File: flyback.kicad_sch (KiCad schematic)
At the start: 47 parts, among them Q2001 FDC86244, U2001 TPS23751PWP, U2002 TCMT1107, U2003 TLV431ACDBZR

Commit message: Updating layout
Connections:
- net T_PRI: now reaches C2003.1, C2004.1, CR2001.1, L2001.2, R2002.1, R2005.1, R2007.1, T2001.1
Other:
- moved on the sheet: C2002
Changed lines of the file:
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@@
 	)
 	(junction
+		(at 95.25 57.15)
+		(diameter 0)
+		(color 0 0 0 0)
+	)
+	(junction
 		(at 195.58 125.73)
 		(diameter 0)
@@
 	)
 	(junction
-		(at 97.79 57.15)
-		(diameter 0)
-		(color 0 0 0 0)
-	)
-	(junction
 		(at 180.34 57.15)
 		(diameter 0)
@@
 	(wire
 		(pts
-			(xy 97.79 40.64) (xy 97.79 44.45)
+			(xy 95.25 40.64) (xy 95.25 44.45)
 		)
 		(stroke
@@
 	(wire
 		(pts
+			(xy 95.25 57.15) (xy 105.41 57.15)
+		)
+		(stroke
+			(width 0)
+			(type default)
+		)
+	)
+	(wire
+		(pts
 			(xy 83.82 139.7) (xy 52.07 139.7)
 		)
@@
 	(wire
 		(pts
-			(xy 102.87 40.64) (xy 97.79 40.64)
+			(xy 102.87 40.64) (xy 95.25 40.64)
 		)
 		(stroke
@@
 	(wire
 		(pts
-			(xy 97.79 57.15) (xy 105.41 57.15)
-		)
-		(stroke
-			(width 0)
-			(type default)
-		)
-	)
-	(wire
-		(pts
 			(xy 50.8 121.92) (xy 50.8 124.46)
 		)
@@
 	(wire
 		(pts
-			(xy 45.72 57.15) (xy 97.79 57.15)
+			(xy 45.72 57.15) (xy 95.25 57.15)
 		)
 		(stroke
@@
 		)
 	)
+	(label "T_PRI"
+		(at 207.01 57.15 0)
+		(fields_autoplaced yes)
+		(effects
+			(font
+				(size 1.27 1.27)
+			)
+			(justify left bottom)
+		)
+	)
 	(global_label "APD"
 		(shape input)
@@
 	(symbol
 		(lib_id "PoE-rescue:C-pspice")
-		(at 97.79 50.8 0)
+		(at 95.25 50.8 0)
 		(mirror x)
 		(unit 1)
@@
 		(dnp no)
 		(property "Reference" "C2002"
-			(at 102.3112 51.9684 0)
+			(at 99.7712 51.9684 0)
 			(effects
 				(font
@@
 		)
 		(property "Value" "22u"
-			(at 102.3112 49.657 0)
+			(at 99.7712 49.657 0)
 			(effects
 				(font
@@
 		)
 		(property "Footprint" "footprints:CAP_WCAP-ASLI_06p3X05p5_WRE"
-			(at 97.79 50.8 0)
+			(at 95.25 50.8 0)
 			(effects
 				(font
@@
 		)
 		(property "Datasheet" "~"
-			(at 97.79 50.8 0)
+			(at 95.25 50.8 0)
 			(effects
 				(font
@@
 		)
 		(property "Description" "CIN1"
-			(at 102.362 47.498 0)
+			(at 99.822 47.498 0)
 			(effects
 				(font

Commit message: Added routing
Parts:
- C2002: value 22u -> 47u; Voltage (none) -> 100V
- C2003: footprint footprints:CAP_WCAP-ASLI_06p3X05p5_WRE -> Capacitor_SMD:C_0805_2012Metric
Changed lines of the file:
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@@
 	)
 	(junction
+		(at 120.65 57.15)
+		(diameter 0)
+		(color 0 0 0 0)
+	)
+	(junction
 		(at 129.54 104.14)
 		(diameter 0)
@@
 	)
 	(junction
-		(at 120.65 57.15)
-		(diameter 0)
-		(color 0 0 0 0)
-	)
-	(junction
 		(at 50.8 113.03)
 		(diameter 0)
@@
 	(wire
 		(pts
-			(xy 120.65 57.15) (xy 129.54 57.15)
+			(xy 113.03 57.15) (xy 120.65 57.15)
 		)
 		(stroke
@@
 	(wire
 		(pts
-			(xy 113.03 57.15) (xy 120.65 57.15)
-		)
-		(stroke
-			(width 0)
-			(type default)
-		)
-	)
-	(wire
-		(pts
 			(xy 50.8 63.5) (xy 50.8 104.14)
 		)
@@
 	(wire
 		(pts
+			(xy 120.65 57.15) (xy 129.54 57.15)
+		)
+		(stroke
+			(width 0)
+			(type default)
+		)
+	)
+	(wire
+		(pts
 			(xy 73.66 40.64) (xy 88.9 40.64)
 		)
@@
 	)
 	(symbol
-		(lib_id "PoE-rescue:C-pspice")
-		(at 120.65 50.8 0)
-		(mirror x)
-		(unit 1)
-		(exclude_from_sim no)
-		(in_bom yes)
-		(on_board yes)
-		(dnp no)
-		(property "Reference" "C2003"
-			(at 125.1712 51.9684 0)
-			(effects
-				(font
-					(size 1.27 1.27)
-				)
-				(justify left)
-			)
-		)
-		(property "Value" "1u"
-			(at 125.1712 49.657 0)
-			(effects
-				(font
-					(size 1.27 1.27)
-				)
-				(justify left)
-			)
-		)
-		(property "Footprint" "footprints:CAP_WCAP-ASLI_06p3X05p5_WRE"
-			(at 120.65 50.8 0)
-			(effects
-				(font
-					(size 1.27 1.27)
-				)
-				(hide yes)
-			)
-		)
-		(property "Datasheet" "~"
-			(at 120.65 50.8 0)
-			(effects
-				(font
-					(size 1.27 1.27)
-				)
-				(hide yes)
-			)
-		)
-		(property "Description" "CIN2"
-			(at 125.476 47.244 0)
-			(effects
-				(font
-					(size 1.27 1.27)
-				)
-				(justify left)
-			)
-		)
-		(pin "1"
-		)
-		(pin "2"
-		)
-		(instances
-			(project "PoE"
-				(path "/e8d70991-5081-4afb-b8c3-5ce9f62355e0/1fdbb5e2-ecd4-47ea-a63c-f2f18c06d291"
-					(reference "C2003")
-					(unit 1)
-				)
-			)
-		)
-	)
-	(symbol
 		(lib_id "power:GND")
 		(at 209.55 115.57 0)
@@
 			)
 		)
-		(property "Value" "22u"
+		(property "Value" "47u"
 			(at 99.7712 49.657 0)
 			(effects
@@
 			)
 		)
+		(property "Voltage" "100V"
+			(at 102.108 54.61 0)
+			(effects
+				(font
+					(size 1.27 1.27)
+				)
+			)
+		)
 		(pin "1"
 		)
@@
 					(unit 1)
 				)
+			)
+		)
+	)
+	(symbol
+		(lib_id "PoE-rescue:C-pspice")
+		(at 120.65 50.8 0)
+		(mirror x)
+		(unit 1)
+		(exclude_from_sim no)
+		(in_bom yes)
+		(on_board yes)
+		(dnp no)
+		(property "Reference" "C2003"
+			(at 125.1712 51.9684 0)
+			(effects
+				(font
+					(size 1.27 1.27)
+				)
+				(justify left)
+			)
+		)
+		(property "Value" "1u"
+			(at 125.1712 49.657 0)
+			(effects
+				(font
+					(size 1.27 1.27)
+				)
+				(justify left)
+			)
+		)
+		(property "Footprint" "Capacitor_SMD:C_0805_2012Metric"
+			(at 120.65 50.8 0)
+			(effects
+				(font
+					(size 1.27 1.27)
+				)
+				(hide yes)
+			)
+		)
+		(property "Datasheet" "~"
+			(at 120.65 50.8 0)
+			(effects
+				(font
+					(size 1.27 1.27)
+				)
+				(hide yes)
+			)
+		)
+		(property "Description" ""
+			(at 120.65 50.8 0)
+			(effects
+				(font
+					(size 1.27 1.27)
+				)
+				(hide yes)
+			)
+		)
+		(pin "1"
+		)
+		(pin "2"
+		)
+		(instances
+			(project "PoE"
+				(path "/e8d70991-5081-4afb-b8c3-5ce9f62355e0/1fdbb5e2-ecd4-47ea-a63c-f2f18c06d291"
+					(reference "C2003")
+					(unit 1)
+				)

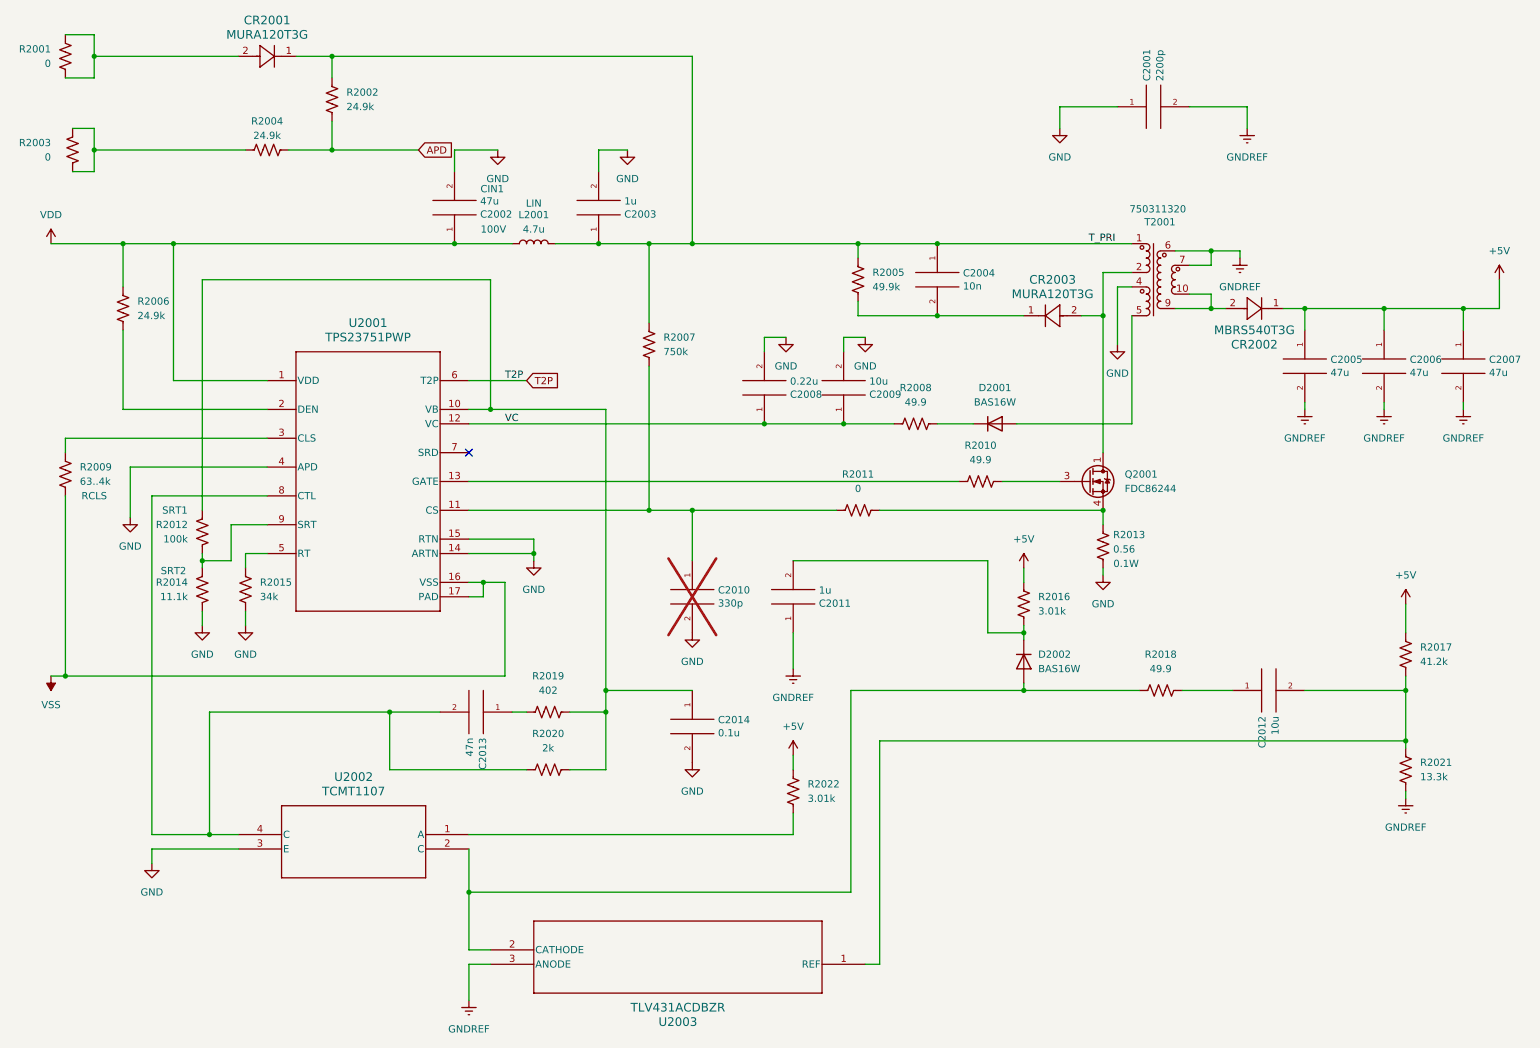
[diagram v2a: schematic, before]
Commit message: Changed main FET
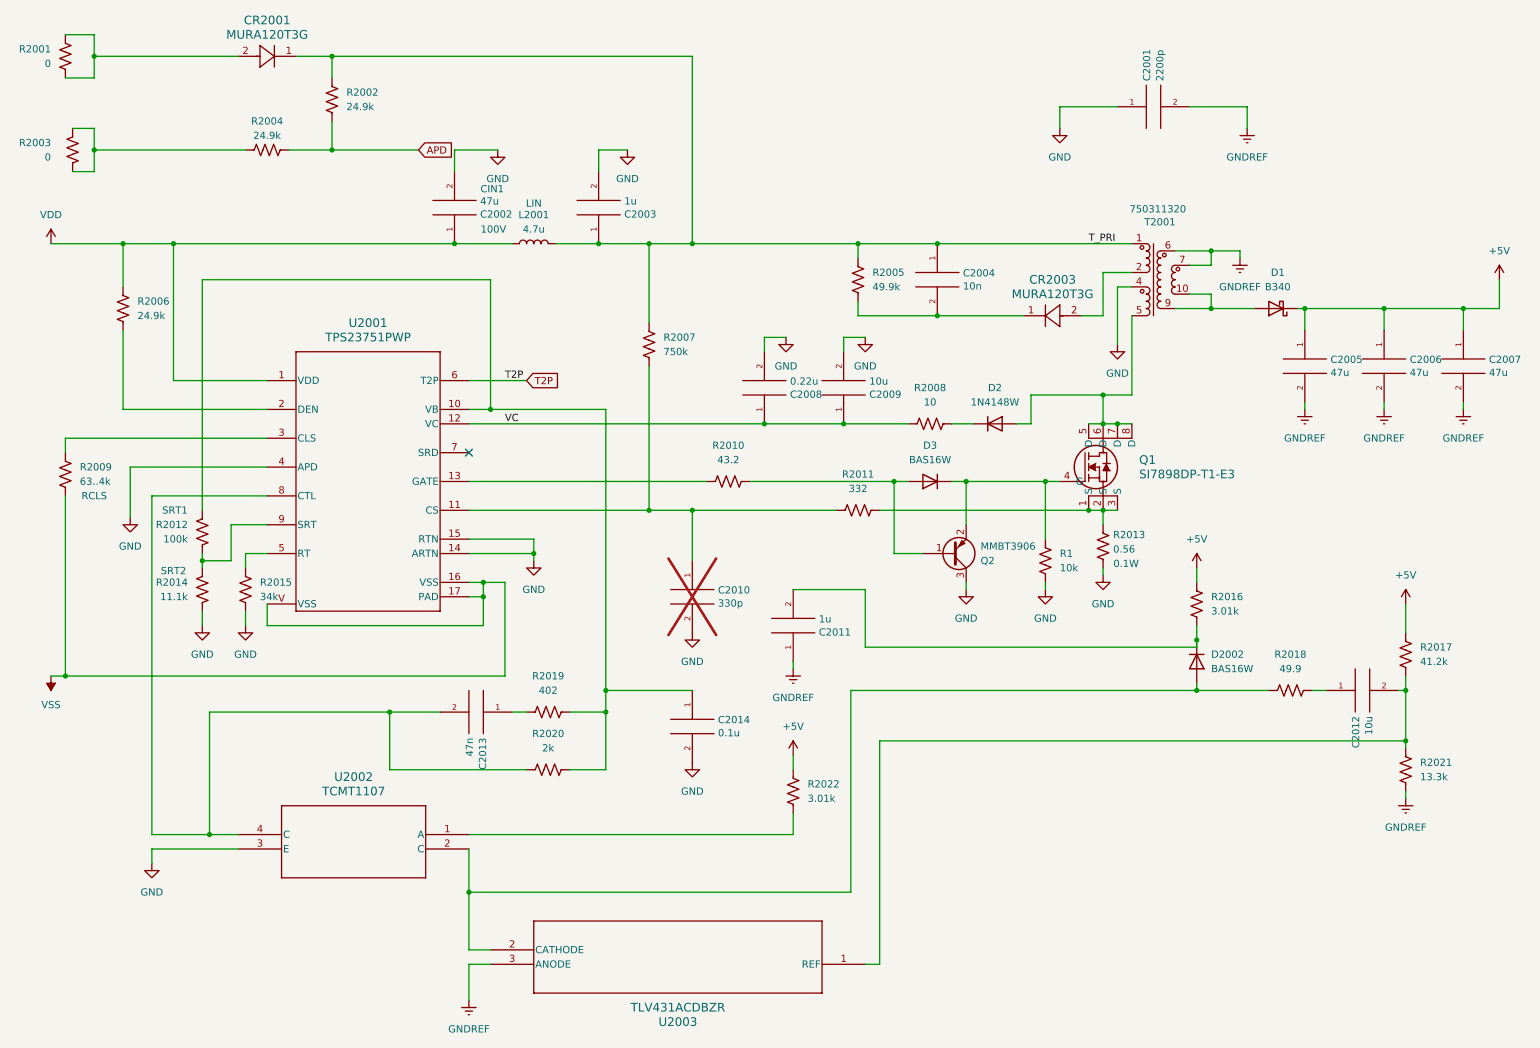
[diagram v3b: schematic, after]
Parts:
- removed CR2002: MBRS540T3G, footprints:DIODE_SMC_7P15X6P25_ONS, symbol MBRS540T3G:MBRS540T3G
- removed D2001: BAS16W, Package_TO_SOT_SMD:SOT-323_SC-70, symbol Diode:BAS16W
- removed Q2001: FDC86244, Package_TO_SOT_SMD:SuperSOT-6, symbol Transistor_FET:FDC86244
- added D1: B340, Diode_SMD:D_SMC, symbol Diode:B340
- added D2: 1N4148W, Diode_SMD:D_SOD-123, symbol Diode:1N4148W
- added D3: BAS16W, Package_TO_SOT_SMD:SOT-323_SC-70, symbol Diode:BAS16W
- added Q1: SI7898DP-T1-E3, footprints:MOSFET_50DP-T1-E3_VIS, symbol SI789DP-T1-E3:SI7898DP-T1-E3
- added Q2: MMBT3906, Package_TO_SOT_SMD:SOT-23, symbol Transistor_BJT:MMBT3906
- added R1: 10k, Resistor_SMD:R_0805_2012Metric, symbol Device:R_US
- R2006, R2007, R2009, R2012: footprint LED_SMD:LED_0805_2012Metric -> Resistor_SMD:R_0805_2012Metric
- R2008: value 49.9 -> 10; footprint LED_SMD:LED_0805_2012Metric -> Resistor_SMD:R_0805_2012Metric
- R2010: value 49.9 -> 43.2; footprint LED_SMD:LED_0805_2012Metric -> Resistor_SMD:R_0805_2012Metric
- R2011: value 0 -> 332; footprint LED_SMD:LED_0805_2012Metric -> Resistor_SMD:R_0805_2012Metric
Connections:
- net +5V: now also D1.1 (K)
- net GND: now also Q2.3 (C), R1.2
- net VSS: now also U2001.V (VSS)
- net at T2001.10, T2001.9: now also D1.2 (A)
- net at R2010.1: now also D3.1 (A), Q2.1 (B)
- net at R2011.1, R2013.1: now also Q1.1 (S), Q1.2 (S), Q1.3 (S)
- net at T2001.5: now also D2.2 (A), Q1.5 (D), Q1.6 (D), Q1.7 (D), Q1.8 (D)
- net at R2008.1: now also D2.1 (K)
- new net: D3.3 (K), Q1.4 (G), Q2.2 (E), R1.1
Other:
- moved on the sheet: C2011, C2012, D2002, R2008, R2010, R2016, R2018

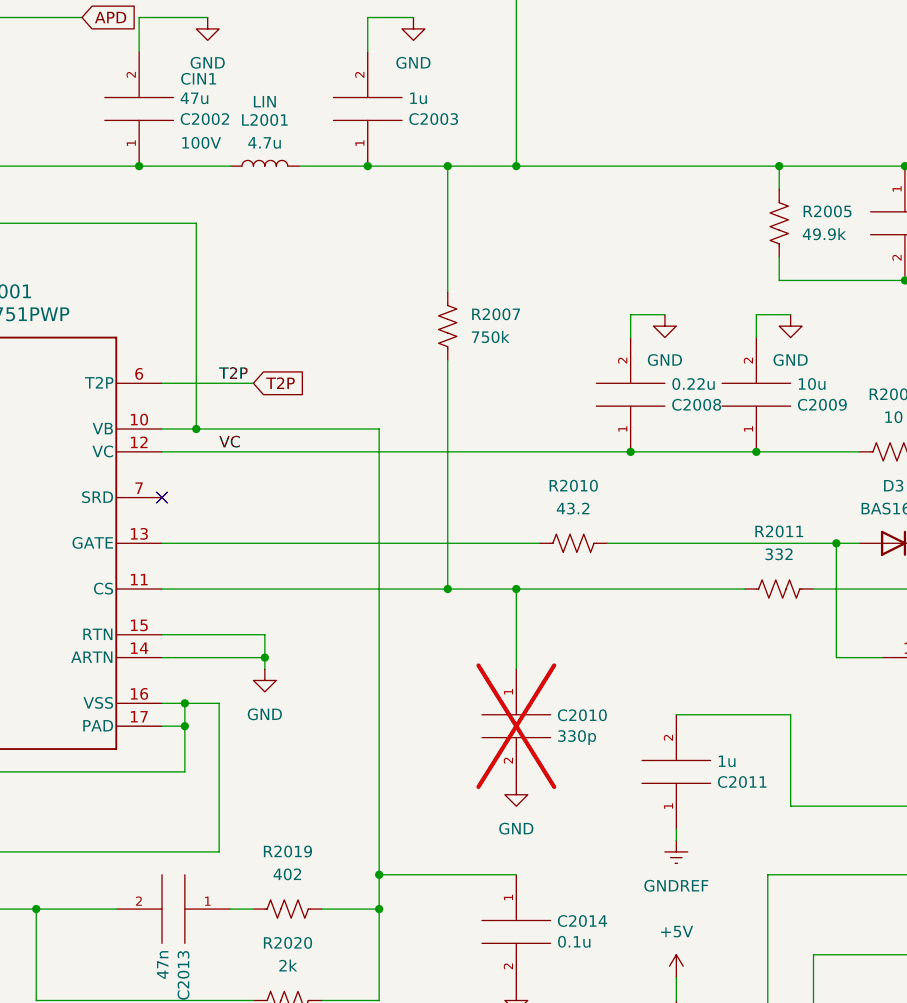
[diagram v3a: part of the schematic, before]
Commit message: Added more routing
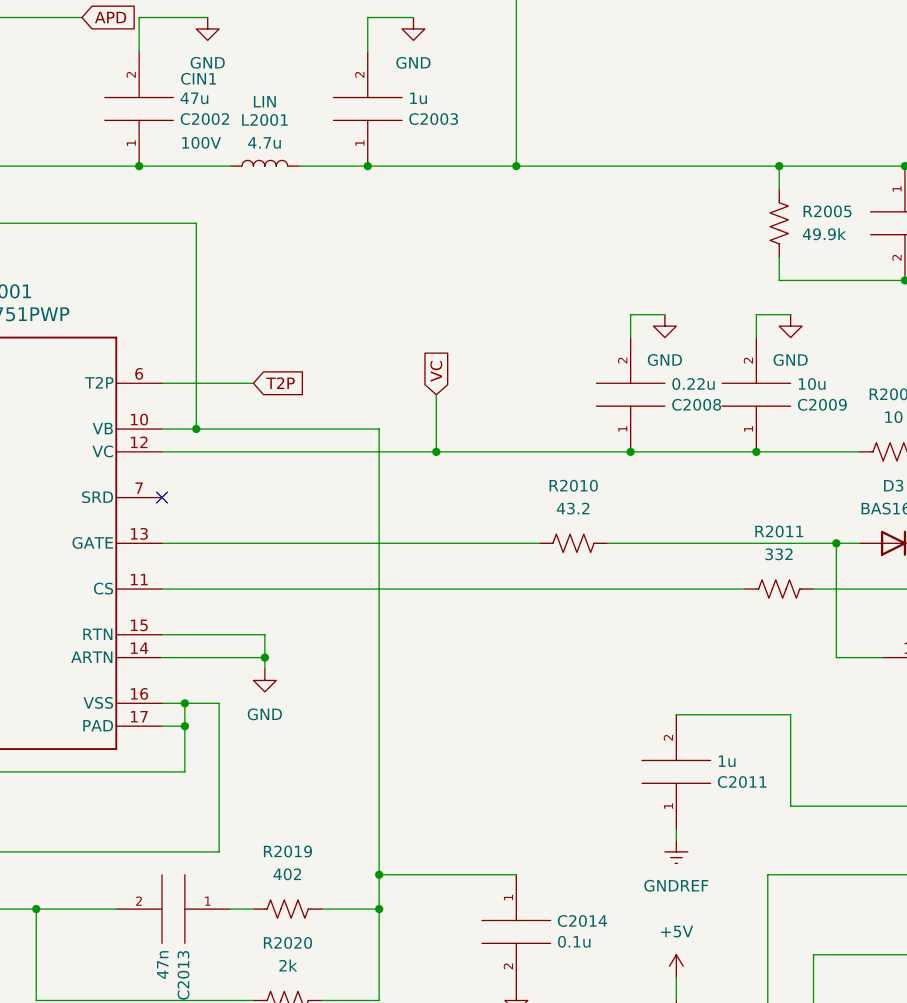
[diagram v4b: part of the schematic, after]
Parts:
- removed C2010: 330p, Capacitor_SMD:C_0805_2012Metric, symbol PoE-rescue:C-pspice
- removed R2007: 750k, Resistor_SMD:R_0805_2012Metric, symbol Device:R_US
